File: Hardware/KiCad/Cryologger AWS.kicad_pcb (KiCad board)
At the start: 2 copper layers, 134.6 x 82.5 mm, 25 parts, among them J1 Screw_Terminal_01x02, J2 Screw_Terminal_01x04, J3 Screw_Terminal_01x04, J4 Screw_Terminal_01x04, U1 Adafruit_LSM303AGR, U10 Pololu_D36V6, U2 Adafruit_DPS310, U3 Adafruit_Feather_Header, U4 Adafruit_Feather_Header, U5 ROCKBLOCK_9603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

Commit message: Fix KiCad design error
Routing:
- net +BATT: track 63.1 -> 62.2 mm
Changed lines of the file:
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@@
     (property "Sheetname" "")
     (attr through_hole)
-    (fp_text reference "R4" (at -2.54 0) (layer "F.SilkS")
+    (fp_text reference "R4" (at 12.7 0) (layer "F.SilkS")
       (effects (font (size 1 1) (thickness 0.15)))
     )
@@
     (property "Sheetname" "")
     (attr through_hole)
-    (fp_text reference "R3" (at -2.54 0) (layer "F.SilkS")
+    (fp_text reference "R3" (at 12.7 0) (layer "F.SilkS")
       (effects (font (size 1 1) (thickness 0.15)))
     )
@@
   (segment (start 215.9 83.82) (end 215.9 93.98) (width 0.8128) (layer "F.Cu") (net 18))
   (segment (start 215.9 83.82) (end 215.9 78.085) (width 0.8128) (layer "F.Cu") (net 18))
+  (segment (start 203.2 124.46) (end 203.2 119.38) (width 0.8128) (layer "B.Cu") (net 18))
+  (segment (start 215.9 112.522) (end 215.9 104.14) (width 0.8128) (layer "B.Cu") (net 18))
   (segment (start 207.9315 129.1915) (end 203.2 124.46) (width 0.8128) (layer "B.Cu") (net 18))
-  (segment (start 203.2 119.38) (end 206.375 116.205) (width 0.8128) (layer "B.Cu") (net 18))
+  (segment (start 203.2 119.38) (end 204.724 117.856) (width 0.8128) (layer "B.Cu") (net 18))
   (segment (start 208.28 129.1915) (end 207.9315 129.1915) (width 0.8128) (layer "B.Cu") (net 18))
-  (segment (start 215.9 114.3) (end 215.9 104.14) (width 0.8128) (layer "B.Cu") (net 18))
-  (segment (start 203.2 124.46) (end 203.2 119.38) (width 0.8128) (layer "B.Cu") (net 18))
-  (segment (start 206.375 116.205) (end 213.995 116.205) (width 0.8128) (layer "B.Cu") (net 18))
-  (segment (start 213.995 116.205) (end 215.9 114.3) (width 0.8128) (layer "B.Cu") (net 18))
+  (segment (start 204.724 117.699481) (end 207.615481 114.808) (width 0.8128) (layer "B.Cu") (net 18))
+  (segment (start 207.615481 114.808) (end 213.614 114.808) (width 0.8128) (layer "B.Cu") (net 18))
+  (segment (start 204.724 117.856) (end 204.724 117.699481) (width 0.8128) (layer "B.Cu") (net 18))
+  (segment (start 213.614 114.808) (end 215.9 112.522) (width 0.8128) (layer "B.Cu") (net 18))
   (segment (start 201.93 101.6) (end 181.61 101.6) (width 0.3048) (layer "B.Cu") (net 19))
   (segment (start 180.34 100.33) (end 177.8 100.33) (width 0.4064) (layer "B.Cu") (net 19))
@@
     (connect_pads (clearance 0.254))
     (min_thickness 0.254) (filled_areas_thickness no)
-    (fill yes (thermal_gap 0.508) (thermal_bridge_width 0.508))
+    (fill (thermal_gap 0.508) (thermal_bridge_width 0.508))
     (polygon
       (pts
@@
     (connect_pads (clearance 0.254))
     (min_thickness 0.254) (filled_areas_thickness no)
-    (fill yes (thermal_gap 0.508) (thermal_bridge_width 0.508))
+    (fill (thermal_gap 0.508) (thermal_bridge_width 0.508))
     (polygon
       (pts

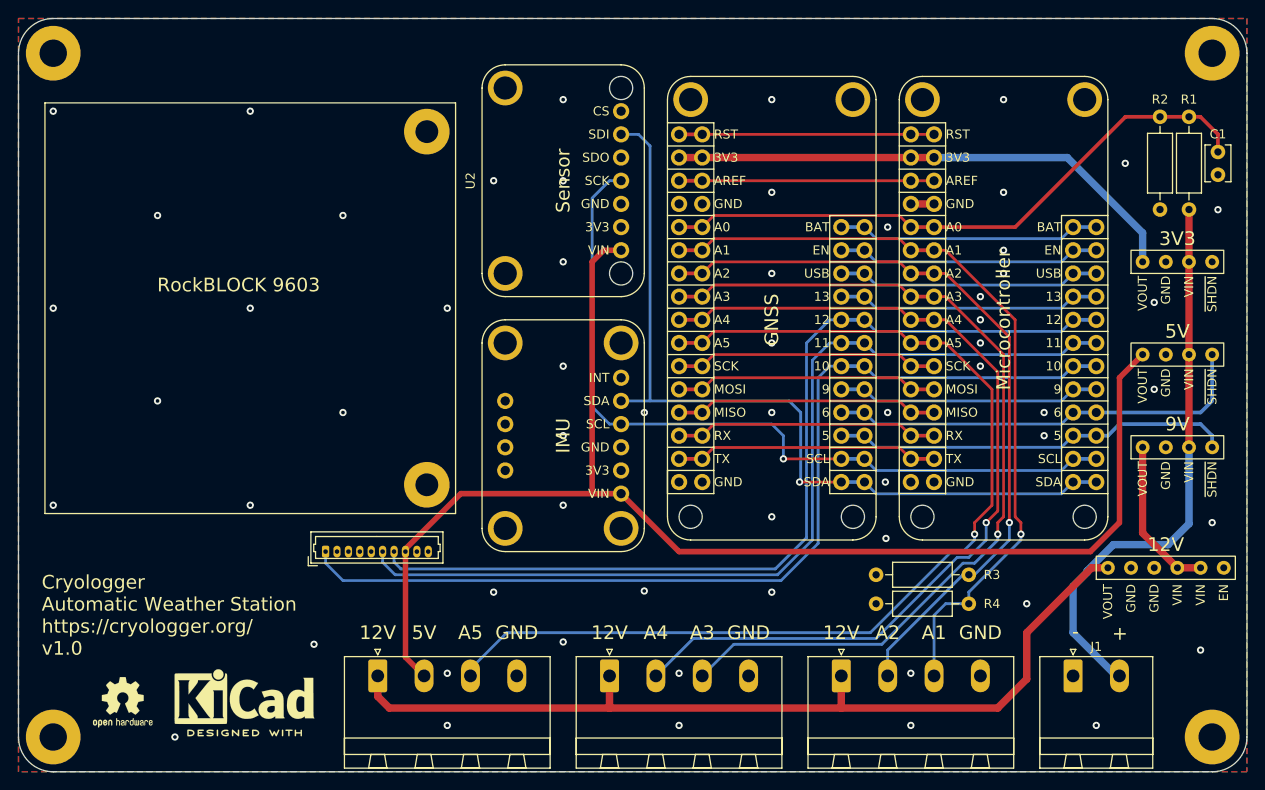
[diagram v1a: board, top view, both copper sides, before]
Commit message: Update PCB to v0.2
Move KiCad and Gerber files into specific version folders.
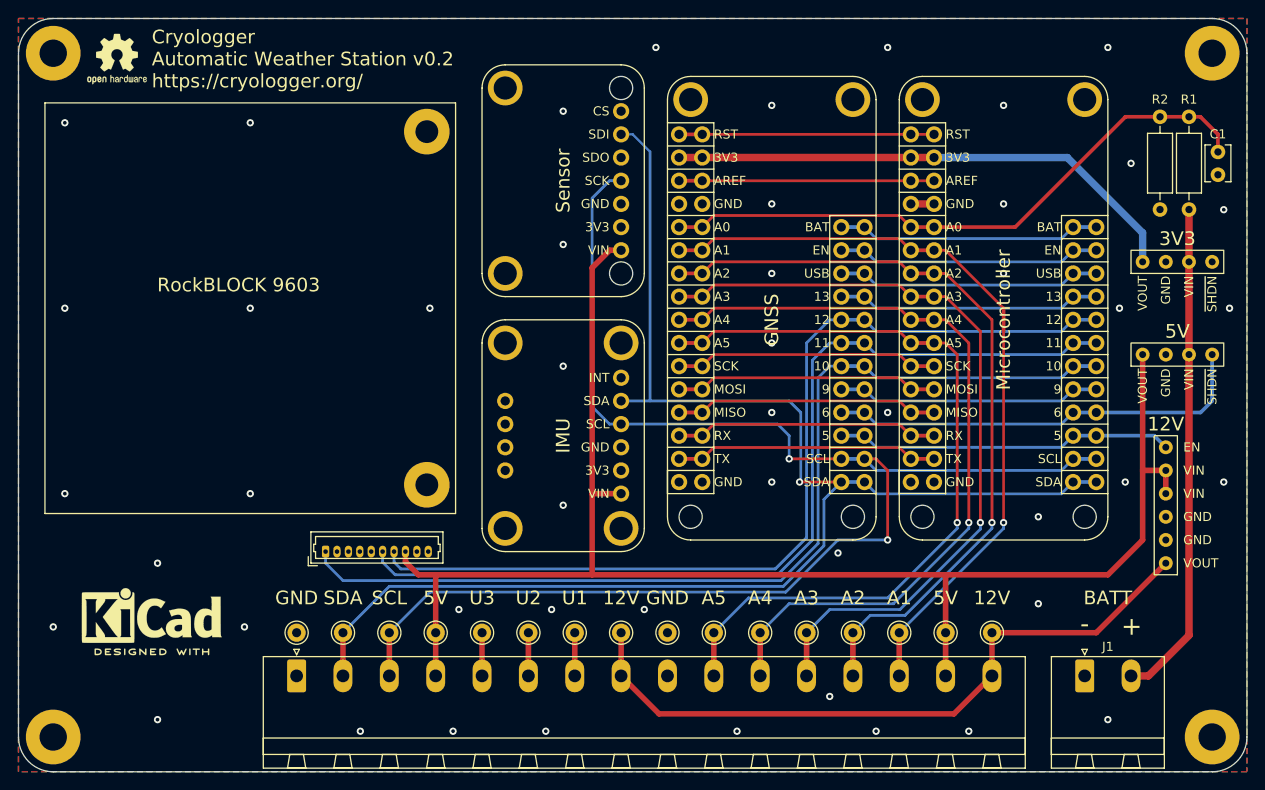
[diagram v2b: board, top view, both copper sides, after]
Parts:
- removed J4: Screw_Terminal_01x04, Connector_Phoenix_MSTB:PhoenixContact_MSTBA_2,5_4-G-5,08_1x04_P5.08mm_Horizontal
- removed R3, R4: 150, Resistor_THT:R_Axial_DIN0207_L6.3mm_D2.5mm_P10.16mm_Horizontal
- removed U10: Pololu_D36V6, Cryologger:Pololu D36V6x
- J2: value Screw_Terminal_01x04 -> Screw_Terminal_01x16; footprint Connector_Phoenix_MSTB:PhoenixContact_MSTBA_2,5_4-G-5,08_1x04_P5.08mm_Horizontal -> Connector_Phoenix_MSTB:PhoenixContact_MSTBA_2,5_16-G-5,08_1x16_P5.08mm_Horizontal
- J3: value Screw_Terminal_01x04 -> Conn_01x16; footprint Connector_Phoenix_MSTB:PhoenixContact_MSTBA_2,5_4-G-5,08_1x04_P5.08mm_Horizontal -> Cryologger:Pin_1.0mm_10.0mm_1x16
- U6, U7: value Pololu_D36V6 -> Pololu_D36V6x; footprint Cryologger:Pololu D36V6x -> Cryologger:Pololu_D36V6x
- U8: footprint Cryologger:RockBLOCK_9603_Footprint -> Cryologger:RockBLOCK_9603
- U9: value U3V40Fx -> Pololu_U3V40Fx; footprint Cryologger:Pololu U3V40Fx -> Cryologger:Pololu_U3V40Fx
- moved REF** 70.5 mm to (98.4, 61.6)
- moved J2 59.7 mm to (118.1, 129.2)
- moved REF** 13.5 mm to (102.2, 122.6)
- moved J3 7.92 mm to (158.8, 124.5)
- moved U9 6.86 mm to (213.4, 110.5)
- moved J1 1.27 mm to (204.5, 129.2)
- moved U6 1.27 mm to (214.6, 85.1)
- moved U7 1.27 mm to (214.6, 95.2)
- turned U1 to 0 degrees
- turned U2 to 0 degrees
- turned U8 to 0 degrees
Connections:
- J2 pad 1: +12V -> GND
- J2 pad 2: A2 -> SDA
- J2 pad 3: A1 -> SCL
- J2 pad 4: GND -> +5V
- J3 pad 1: +12V -> GND
- J3 pad 2: A4 -> SDA
- J3 pad 3: A3 -> SCL
- J3 pad 4: GND -> +5V
- U9 pad 3: +9V -> +5V
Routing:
- net SCL: track 87.0 -> 161.8 mm, vias 1 -> 2
- net SDA: track 93.1 -> 162.5 mm
- net A5: track 116.6 -> 87.9 mm
- net +12V: track 99.2 -> 76.4 mm
- net +9V: track 17.3 -> 0.00 mm
- net +5V: track 159.8 -> 173.1 mm
- net A4: track 99.6 -> 87.1 mm
- net A3: track 98.4 -> 86.4 mm
- net +BATT: track 62.2 -> 54.9 mm
- net D5: track 44.0 -> 37.1 mm
- net NC3: track 0.00 -> 4.73 mm
- net NC2: track 0.00 -> 4.73 mm
- net NC1: track 0.00 -> 4.73 mm
- net A2: track 83.5 -> 85.6 mm
- net A1: track 85.8 -> 84.9 mm
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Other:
- board text added: "BATT"
- board text added: "Cryologger Automatic Weather Station v0.2 https://cryologger.org/"
- board text added: "SCL"
- board text added: "SDA"
- board text added: "U1"
- board text added: "U2"
- board text added: "U3"
- board text removed: "9V"
- board text removed: "Cryologger Automatic Weather Station https://cryologger.org/ v1.0"
